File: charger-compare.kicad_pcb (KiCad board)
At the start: 4 copper layers, 52.5 x 80 mm, 109 parts, among them J1 2.5x5.5mm, J3 Batt, J4 2.5x5.5mm, J5 TYPE-C16PIN, J6 TYPE-C16PIN, J7 TagConnect 2030-NL, Q1 HL2304, SW1 MS-22C01-G010, SW2 TS-1088-AR02016, U1 BQ25792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

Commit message: More fixes
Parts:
- D3, D4: footprint Diode_SMD:D_SOD-123 -> Diode_SMD:D_SOD-323
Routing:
- net GNDPWR: track 103.4 -> 107.9 mm
- net /I2C Ctrl/5V_BS: track 4.49 -> 5.69 mm

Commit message: Fix reference
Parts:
- renumbered REF** to LBL1
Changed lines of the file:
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@@
 		(layer "B.Cu")
 		(at 168.119922 69.095066 180)
-		(property "Reference" "REF**"
+		(property "Reference" "LBL1"
 			(at 2.089922 5.59 0)
 			(unlocked yes)

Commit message: Set LED resistors
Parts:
- R1, R25, R26: value 3.3k -> 1.2k
- R21, R23: value R -> 16k
- R22, R24, R33: value R -> 4.7k
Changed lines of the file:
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@@
 			)
 		)
-		(property "Value" "R"
+		(property "Value" "4.7k"
 			(at 0 1.17 0)
 			(layer "F.Fab")
@@
 			)
 		)
-		(property "Value" "R"
+		(property "Value" "4.7k"
 			(at 0 1.17 90)
 			(layer "F.Fab")
@@
 			)
 		)
-		(property "Value" "R"
+		(property "Value" "16k"
 			(at 0 1.17 0)
 			(layer "F.Fab")
@@
 			)
 		)
-		(property "Value" "R"
+		(property "Value" "16k"
 			(at 0 1.17 0)
 			(layer "F.Fab")
@@
 			)
 		)
-		(property "Value" "3.3k"
+		(property "Value" "1.2k"
 			(at 0 1.17 0)
 			(layer "F.Fab")
@@
 			)
 		)
-		(property "Value" "3.3k"
+		(property "Value" "1.2k"
 			(at 0 1.17 0)
 			(layer "F.Fab")
@@
 			)
 		)
-		(property "Value" "R"
+		(property "Value" "4.7k"
 			(at 0 1.17 0)
 			(layer "F.Fab")
@@
 			)
 		)
-		(property "Value" "3.3k"
+		(property "Value" "1.2k"
 			(at 0 1.17 90)
 			(layer "F.Fab")

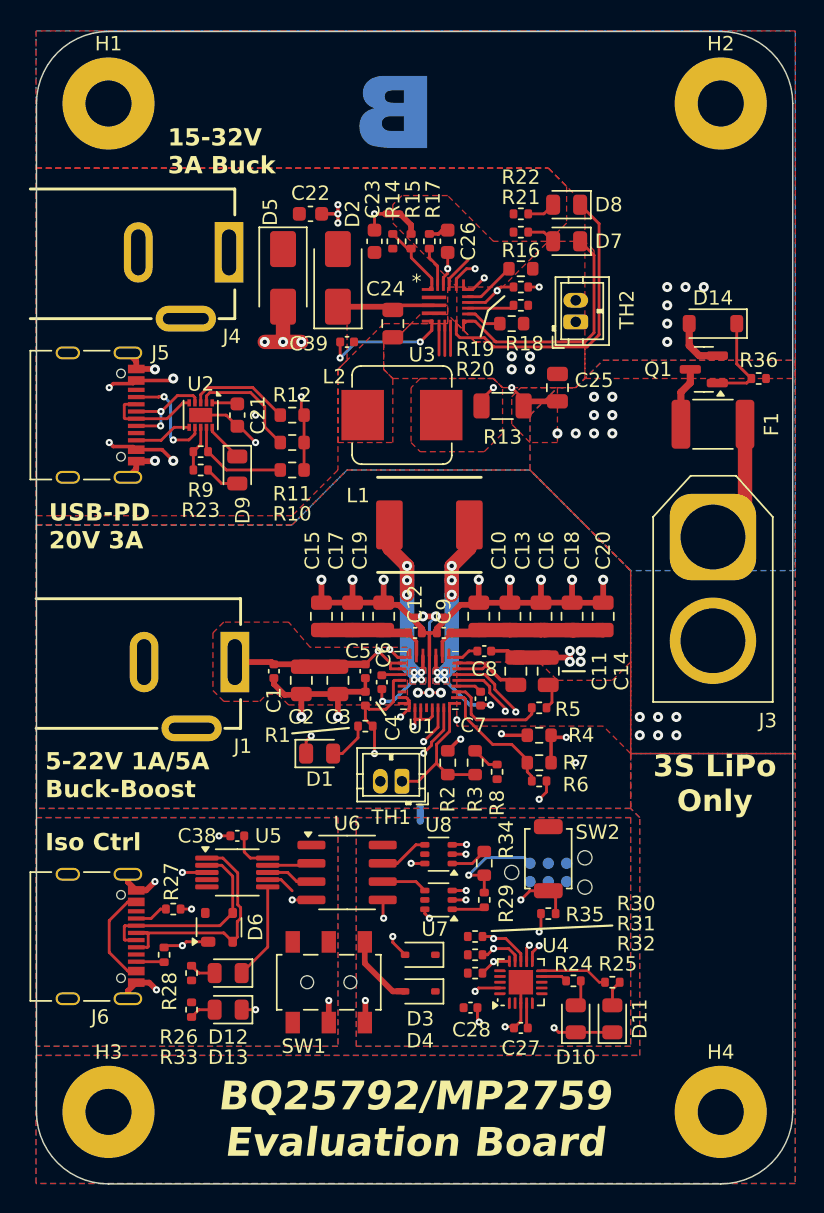
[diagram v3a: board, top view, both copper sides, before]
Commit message: Switch to JST-PH connectors Add Sheet titles
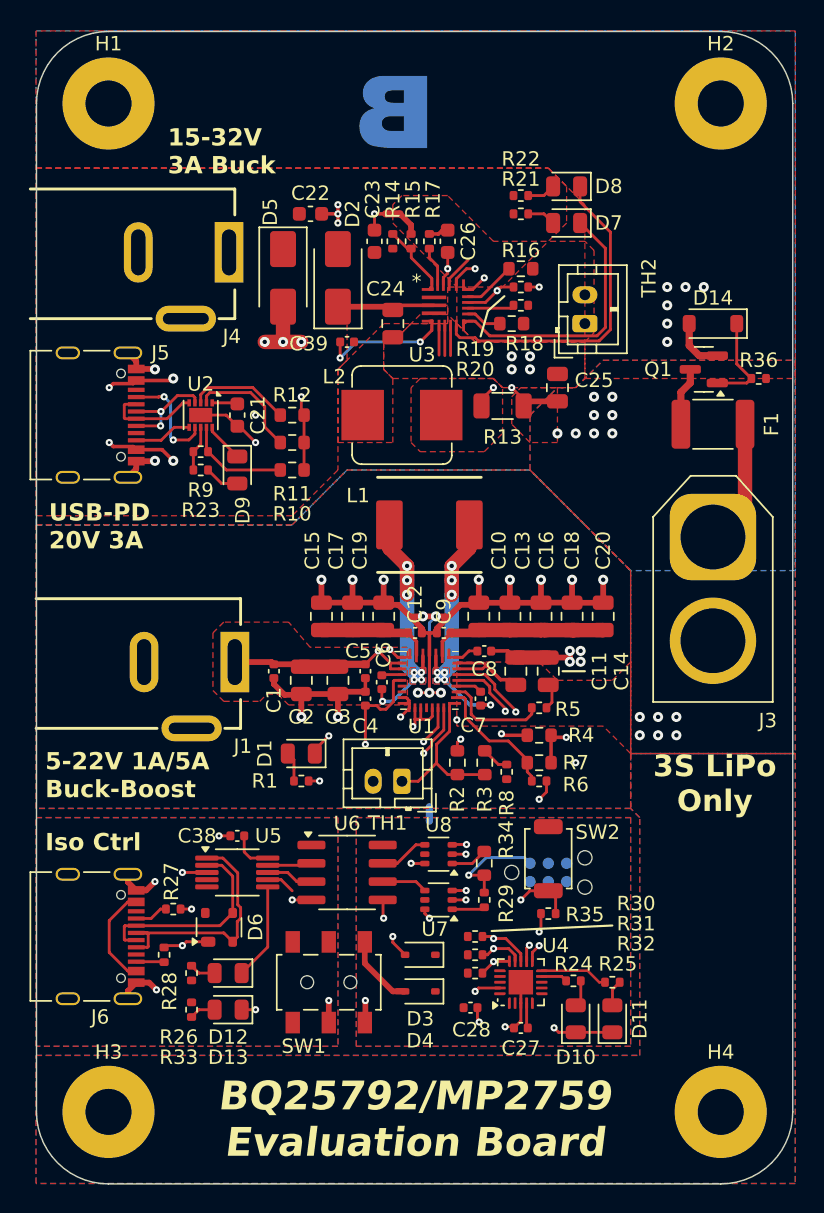
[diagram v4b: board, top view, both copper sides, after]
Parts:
- TH1, TH2: footprint Connector_JST:JST_ZH_B2B-ZR_1x02_P1.50mm_Vertical -> Connector_JST:JST_PH_B2B-PH-K_1x02_P2.00mm_Vertical
- moved R1 5.85 mm to (159.4, 113.0)
- moved D1 1.27 mm to (159.4, 111.1), turned to 180 degrees
- moved D8 1.27 mm to (177.8, 71.8)
- moved R21 1.27 mm to (174.6, 73.7)
- moved D7 1.27 mm to (177.8, 74.3)
- moved R22 1.27 mm to (174.6, 72.4)
- moved R3 0.67 mm to (172.1, 111.8)
- moved R8 0.67 mm to (173.6, 112.4)
- moved R2 0.67 mm to (170.2, 111.8)
- moved TH2 0.65 mm to (179.1, 81.3)
- moved NT1 0.64 mm to (168.3, 115.3)
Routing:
- net /BQ25792 Buck-boost/REGN: track 12.3 -> 16.0 mm, vias 4 -> 5
- net /MP2759 Buck/~{STAT}: track 20.8 -> 22.6 mm
- net /MP2759 Buck/~{ACOK}: track 16.4 -> 18.2 mm
- net /BQ25792 Buck-boost/STAT: track 13.6 -> 12.6 mm
- net Net-(D1-A): track 2.99 -> 2.08 mm
- net Net-(U3-NTC): track 9.78 -> 10.6 mm
- net Net-(U1-TS): track 10.2 -> 10.9 mm

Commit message: Action review feedback
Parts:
- added R37: 0R, Resistor_SMD:R_1206_3216Metric, F.Cu at (154.3, 84.5)
- U6: value ADuM1201AR -> ADuM1201ARZ
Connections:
- C22 pad 1: /VBUS -> /MP2759 Buck/VIN
- C23 pad 1: /VBUS -> /MP2759 Buck/VIN
- D2 pad 2: /VBUS -> /MP2759 Buck/VIN
- D5 pad 1: /VBUS -> /MP2759 Buck/VIN
- J4 pad 1: /VBUS -> /MP2759 Buck/VIN
- R14 pad 1: /VBUS -> /MP2759 Buck/VIN
- R21 pad 2: /VBUS -> /MP2759 Buck/VIN
- R22 pad 2: /VBUS -> /MP2759 Buck/VIN
- U3 pad 1: /VBUS -> /MP2759 Buck/VIN
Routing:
- net /MP2759 Buck/VIN: track 0.00 -> 2.87 mm, vias 0 -> 2
- net /VBUS: track 14.6 -> 15.9 mm, vias 5 -> 6
- added copper zone on F.Cu, net /MP2759 Buck/VIN
- added copper zone on In1.Cu, net /MP2759 Buck/VIN
